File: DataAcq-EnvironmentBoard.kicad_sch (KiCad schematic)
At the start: 13 parts, among them J1 CAN Output, J2 CAN Input, U1 SHT45, U2 FS3000-1005, U3 LMT87DCK, U4 Daughterboard Connector

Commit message: initial layout/routing
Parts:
- added MH1, MH2, MH3, MH4: M.3, MountingHole:MountingHole_3mm, symbol Mechanical:MountingHole
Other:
- moved on the sheet: C1, C2, C3, C4, C5, C6, J1, J2, R1, U1, U2, U3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

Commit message: layout again
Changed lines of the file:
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@@
 	(wire
 		(pts
-			(xy 95.25 115.57) (xy 106.68 115.57)
+			(xy 101.6 115.57) (xy 106.68 115.57)
 		)
 		(stroke
@@
 	(wire
 		(pts
+			(xy 173.99 123.19) (xy 186.69 123.19)
+		)
+		(stroke
+			(width 0)
+			(type default)
+		)
+	)
+	(wire
+		(pts
 			(xy 151.13 60.96) (xy 166.37 60.96)
 		)
@@
 	(wire
 		(pts
-			(xy 177.8 123.19) (xy 186.69 123.19)
-		)
-		(stroke
-			(width 0)
-			(type default)
-		)
-	)
-	(wire
-		(pts
 			(xy 95.25 128.27) (xy 106.68 128.27)
 		)
@@
 	(wire
 		(pts
-			(xy 158.75 63.5) (xy 151.13 63.5)
+			(xy 173.99 139.7) (xy 186.69 139.7)
 		)
 		(stroke
@@
 	(wire
 		(pts
-			(xy 85.09 58.42) (xy 85.09 59.69)
+			(xy 158.75 63.5) (xy 151.13 63.5)
 		)
 		(stroke
@@
 	(wire
 		(pts
-			(xy 97.79 69.85) (xy 107.95 69.85)
+			(xy 85.09 58.42) (xy 85.09 59.69)
 		)
 		(stroke
@@
 	(wire
 		(pts
-			(xy 177.8 139.7) (xy 186.69 139.7)
+			(xy 97.79 69.85) (xy 107.95 69.85)
 		)
 		(stroke
@@
 		)
 	)
-	(label "+12V_In"
-		(at 177.8 123.19 0)
-		(fields_autoplaced yes)
-		(effects
-			(font
-				(size 1.27 1.27)
-			)
-			(justify left bottom)
-		)
-	)
 	(label "TEMP_OUT"
 		(at 228.6 62.23 0)
@@
 		)
 	)
-	(label "+12V_In"
-		(at 95.25 118.11 0)
-		(fields_autoplaced yes)
-		(effects
-			(font
-				(size 1.27 1.27)
-			)
-			(justify left bottom)
-		)
-	)
 	(label "PA1(ADC)"
 		(at 95.25 120.65 0)
@@
 	)
 	(symbol
+		(lib_id "power:+12V")
+		(at 95.25 118.11 90)
+		(unit 1)
+		(exclude_from_sim no)
+		(in_bom yes)
+		(on_board yes)
+		(dnp no)
+		(fields_autoplaced yes)
+		(property "Reference" "#PWR017"
+			(at 99.06 118.11 0)
+			(effects
+				(font
+					(size 1.27 1.27)
+				)
+				(hide yes)
+			)
+		)
+		(property "Value" "+12V_In"
+			(at 91.44 118.1099 90)
+			(effects
+				(font
+					(size 1.27 1.27)
+				)
+				(justify left)
+			)
+		)
+		(property "Footprint" ""
+			(at 95.25 118.11 0)
+			(effects
+				(font
+					(size 1.27 1.27)
+				)
+				(hide yes)
+			)
+		)
+		(property "Datasheet" ""
+			(at 95.25 118.11 0)
+			(effects
+				(font
+					(size 1.27 1.27)
+				)
+				(hide yes)
+			)
+		)
+		(property "Description" "Power symbol creates a global label with name \"+12V\""
+			(at 95.25 118.11 0)
+			(effects
+				(font
+					(size 1.27 1.27)
+				)
+				(hide yes)
+			)
+		)
+		(pin "1"
+		)
+		(instances
+			(project ""
+				(path "/bc5fb1f8-c603-414b-89d1-18cc156ddb66"
+					(reference "#PWR017")
+					(unit 1)
+				)
+			)
+		)
+	)
+	(symbol
 		(lib_id "power:+3.3V")
 		(at 152.4 133.35 270)
@@
 	)
 	(symbol
+		(lib_id "power:+12V")
+		(at 173.99 123.19 90)
+		(unit 1)
+		(exclude_from_sim no)
+		(in_bom yes)
+		(on_board yes)
+		(dnp no)
+		(fields_autoplaced yes)
+		(property "Reference" "#PWR018"
+			(at 177.8 123.19 0)
+			(effects
+				(font
+					(size 1.27 1.27)
+				)
+				(hide yes)
+			)
+		)
+		(property "Value" "+12V_In"
+			(at 170.18 123.1899 90)
+			(effects
+				(font
+					(size 1.27 1.27)
+				)
+				(justify left)
+			)
+		)
+		(property "Footprint" ""
+			(at 173.99 123.19 0)
+			(effects
+				(font
+					(size 1.27 1.27)
+				)
+				(hide yes)
+			)
+		)
+		(property "Datasheet" ""
+			(at 173.99 123.19 0)
+			(effects
+				(font
+					(size 1.27 1.27)
+				)
+				(hide yes)
+			)
+		)
+		(property "Description" "Power symbol creates a global label with name \"+12V\""
+			(at 173.99 123.19 0)
+			(effects
+				(font
+					(size 1.27 1.27)
+				)
+				(hide yes)
+			)
+		)
+		(pin "1"
+		)
+		(instances
+			(project "DataAcq-EnvironmentBoard"
+				(path "/bc5fb1f8-c603-414b-89d1-18cc156ddb66"
+					(reference "#PWR018")
+					(unit 1)
+				)
+			)
+		)
+	)
+	(symbol
 		(lib_id "power:VDDA")
 		(at 96.52 133.35 90)
@@
 	(symbol
 		(lib_id "power:GNDPWR")
-		(at 95.25 115.57 270)
+		(at 101.6 115.57 270)
 		(unit 1)
 		(exclude_from_sim no)
@@
 		(fields_autoplaced yes)
 		(property "Reference" "#PWR08"
-			(at 90.17 115.57 0)
+			(at 96.52 115.57 0)
 			(effects
 				(font
@@
 		)
 		(property "Value" "GNDPWR"
-			(at 91.44 115.4429 90)
+			(at 97.79 115.4429 90)
 			(effects
 				(font
@@
 		)
 		(property "Footprint" ""
-			(at 93.98 115.57 0)
+			(at 100.33 115.57 0)
 			(effects
 				(font
@@
 		)
 		(property "Datasheet" ""
-			(at 93.98 115.57 0)
+			(at 100.33 115.57 0)
 			(effects
 				(font
@@
 		)
 		(property "Description" "Power symbol creates a global label with name \"GNDPWR\" , global ground"
-			(at 95.25 115.57 0)
+			(at 101.6 115.57 0)
 			(effects
 				(font
@@
 					(unit 1)
 				)
+			)
+		)
+	)
+	(symbol
+		(lib_id "power:+12V")
+		(at 173.99 139.7 90)
+		(unit 1)
+		(exclude_from_sim no)
+		(in_bom yes)
+		(on_board yes)
+		(dnp no)
+		(fields_autoplaced yes)
+		(property "Reference" "#PWR019"
+			(at 177.8 139.7 0)
+			(effects
+				(font
+					(size 1.27 1.27)
+				)
+				(hide yes)
+			)
+		)
+		(property "Value" "+12V_In"
+			(at 170.18 139.6999 90)
+			(effects
+				(font
+					(size 1.27 1.27)
+				)
+				(justify left)
+			)
+		)
+		(property "Footprint" ""
+			(at 173.99 139.7 0)
+			(effects
+				(font
+					(size 1.27 1.27)
+				)
+				(hide yes)
+			)
+		)
+		(property "Datasheet" ""
+			(at 173.99 139.7 0)
+			(effects
+				(font
+					(size 1.27 1.27)
+				)
+				(hide yes)
+			)
+		)
+		(property "Description" "Power symbol creates a global label with name \"+12V\""
+			(at 173.99 139.7 0)
+			(effects
+				(font
+					(size 1.27 1.27)
+				)
+				(hide yes)
+			)
+		)
+		(pin "1"
+		)
+		(instances
+			(project "DataAcq-EnvironmentBoard"
+				(path "/bc5fb1f8-c603-414b-89d1-18cc156ddb66"
+					(reference "#PWR019")
+					(unit 1)
+				)

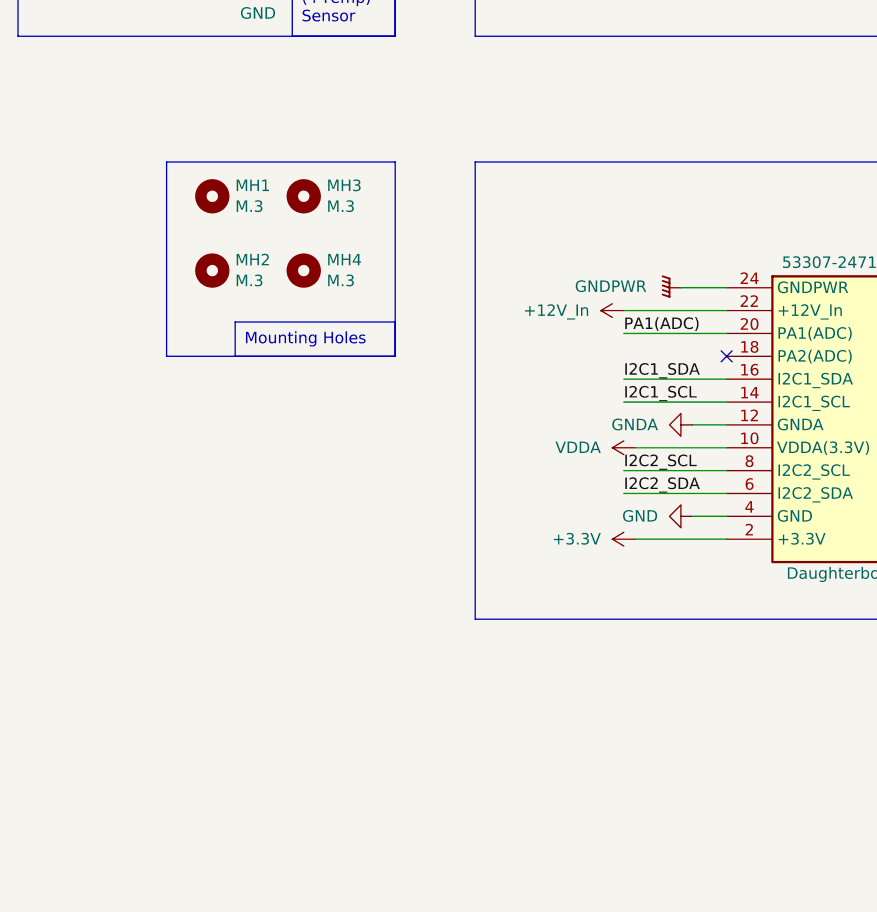
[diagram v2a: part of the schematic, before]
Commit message: add LEDs/testpoints to sch
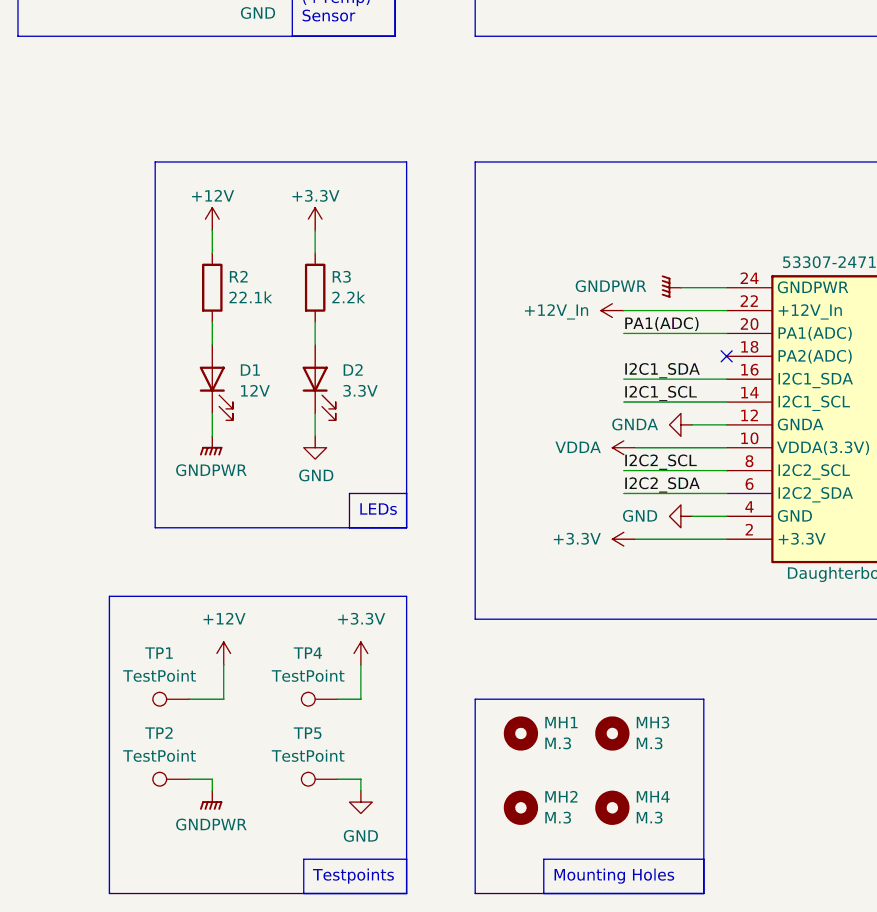
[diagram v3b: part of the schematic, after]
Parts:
- added D1: 12V, LED_SMD:LED_0805_2012Metric, symbol Device:LED
- added D2: 3.3V, LED_SMD:LED_0805_2012Metric, symbol Device:LED
- added R2: 22.1k, Resistor_SMD:R_0805_2012Metric, symbol Device:R
- added R3: 2.2k, Resistor_SMD:R_0805_2012Metric, symbol Device:R
- added TP1, TP2, TP4, TP5: TestPoint, Connector_PinHeader_2.54mm:PinHeader_1x01_P2.54mm_Vertical, symbol Connector:TestPoint
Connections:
- net +3.3V: now also R3.1, TP4.1
- net GND: now also D2.1 (K), TP5.1
- net GNDPWR: now also D1.1 (K), TP2.1
- new net: D1.2 (A), R2.2
- new net: D2.2 (A), R3.2
- new net +12V: R2.1, TP1.1
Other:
- moved on the sheet: MH1, MH2, MH3, MH4

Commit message: test points
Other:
- moved on the sheet: D1, D2, J1, J2, MH1, MH2, MH3, MH4, R2, R3, TP1, TP2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

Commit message: part numbers smh
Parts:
- C1, C2, C3, C5: P/N (none) -> C0805C104M5RACTU
- C4, C6: P/N (none) -> C0805C105K5PACTU
- J1, J2: P/N (none) -> 436500244
- R1: value 800 -> 1k; P/N (none) -> CRCW08051K00FKEAC
- U1: P/N (none) -> SHT45-AD1B-R3
- U2: P/N (none) -> FS3000-1005
- U3: P/N (none) -> LMT87QDCKRQ1
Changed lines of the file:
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@@
 			)
 		)
+		(property "P/N" "436500244"
+			(at 191.77 130.81 0)
+			(effects
+				(font
+					(size 1.27 1.27)
+				)
+				(hide yes)
+			)
+		)
 		(pin "2"
 		)
@@
 			)
 		)
+		(property "P/N" "C0805C104M5RACTU"
+			(at 196.85 57.15 0)
+			(effects
+				(font
+					(size 1.27 1.27)
+				)
+				(hide yes)
+			)
+		)
 		(pin "1"
 		)
@@
 			)
 		)
+		(property "P/N" "C0805C105K5PACTU"
+			(at 250.19 68.58 0)
+			(effects
+				(font
+					(size 1.27 1.27)
+				)
+				(hide yes)
+			)
+		)
 		(pin "1"
 		)
@@
 			)
 		)
+		(property "P/N" "C0805C104M5RACTU"
+			(at 170.18 59.69 0)
+			(effects
+				(font
+					(size 1.27 1.27)
+				)
+				(hide yes)
+			)
+		)
 		(pin "1"
 		)
@@
 			)
 		)
-		(property "Value" "800"
+		(property "Value" "1k"
 			(at 242.57 64.516 90)
 			(effects
@@
 			)
 		)
+		(property "P/N" "CRCW08051K00FKEAC"
+			(at 242.57 62.23 0)
+			(effects
+				(font
+					(size 1.27 1.27)
+				)
+				(hide yes)
+			)
+		)
 		(pin "1"
 		)
@@
 			)
 		)
+		(property "P/N" "C0805C105K5PACTU"
+			(at 158.75 71.12 0)
+			(effects
+				(font
+					(size 1.27 1.27)
+				)
+				(hide yes)
+			)
+		)
 		(pin "1"
 		)
@@
 			)
 		)
+		(property "P/N" "LMT87QDCKRQ1"
+			(at 218.44 62.23 0)
+			(effects
+				(font
+					(size 1.27 1.27)
+				)
+				(hide yes)
+			)
+		)
 		(pin "3"
 		)
@@
 			)
 		)
+		(property "P/N" "SHT45-AD1B-R3 "
+			(at 52.07 69.85 0)
+			(effects
+				(font
+					(size 1.27 1.27)
+				)
+				(hide yes)
+			)
+		)
 		(pin "2"
 		)
@@
 			)
 		)
+		(property "P/N" "C0805C104M5RACTU"
+			(at 85.09 63.5 0)
+			(effects
+				(font
+					(size 1.27 1.27)
+				)
+				(hide yes)
+			)
+		)
 		(pin "2"
 		)
@@
 			)
 		)
+		(property "P/N" "436500244"
+			(at 191.77 114.3 0)
+			(effects
+				(font
+					(size 1.27 1.27)
+				)
+				(hide yes)
+			)
+		)
 		(pin "2"
 		)
@@
 			)
 		)
+		(property "P/N" "C0805C104M5RACTU"
+			(at 97.79 63.5 0)
+			(effects
+				(font
+					(size 1.27 1.27)
+				)
+				(hide yes)
+			)
+		)
 		(pin "2"
 		)
@@
 				(hide yes)
 			)
+		)
+		(property "P/N" "FS3000-1005"
+			(at 123.19 55.88 0)
+			(effects
+				(font
+					(size 1.27 1.27)
+				)
+				(hide yes)
+			)

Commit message: dumbass labels
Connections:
- net +12V is gone; now on net +12V_In: R2.1, TP1.1
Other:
- moved on the sheet: J1, J2, U4

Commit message: cap
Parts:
- added C7: 0.1uF, Capacitor_SMD:C_0805_2012Metric, symbol Device:C
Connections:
- net +3.3V: now also C7.1
- net GND: now also C7.2
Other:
- moved on the sheet: U1
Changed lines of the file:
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@@
 	)
 	(junction
+		(at 52.07 78.74)
+		(diameter 0)
+		(color 0 0 0 0)
+	)
+	(junction
 		(at 215.9 49.53)
 		(diameter 0)
 		(color 0 0 0 0)
 	)
+	(junction
+		(at 52.07 60.96)
+		(diameter 0)
+		(color 0 0 0 0)
+	)
 	(no_connect
 		(at 142.24 137.16)
@@
 	(wire
 		(pts
+			(xy 52.07 60.96) (xy 52.07 62.23)
+		)
+		(stroke
+			(width 0)
+			(type default)
+		)
+	)
+	(wire
+		(pts
 			(xy 172.72 116.84) (xy 185.42 116.84)
 		)
@@
 	(wire
 		(pts
-			(xy 34.29 72.39) (xy 44.45 72.39)
+			(xy 31.75 72.39) (xy 41.91 72.39)
 		)
 		(stroke
@@
 	(wire
 		(pts
-			(xy 54.61 77.47) (xy 54.61 80.01)
+			(xy 52.07 77.47) (xy 52.07 78.74)
+		)
+		(stroke
+			(width 0)
+			(type default)
+		)
+	)
+	(wire
+		(pts
+			(xy 59.69 78.74) (xy 52.07 78.74)
 		)
 		(stroke
@@
 	(wire
 		(pts
+			(xy 59.69 73.66) (xy 59.69 78.74)
+		)
+		(stroke
+			(width 0)
+			(type default)
+		)
+	)
+	(wire
+		(pts
+			(xy 59.69 66.04) (xy 59.69 60.96)
+		)
+		(stroke
+			(width 0)
+			(type default)
+		)
+	)
+	(wire
+		(pts
 			(xy 250.19 62.23) (xy 261.62 62.23)
 		)
@@
 	(wire
 		(pts
-			(xy 34.29 67.31) (xy 44.45 67.31)
+			(xy 31.75 67.31) (xy 41.91 67.31)
 		)
 		(stroke
@@
 	(wire
 		(pts
+			(xy 59.69 60.96) (xy 52.07 60.96)
+		)
+		(stroke
+			(width 0)
+			(type default)
+		)
+	)
+	(wire
+		(pts
 			(xy 97.79 55.88) (xy 123.19 55.88)
 		)
@@
 	(wire
 		(pts
+			(xy 52.07 78.74) (xy 52.07 80.01)
+		)
+		(stroke
+			(width 0)
+			(type default)
+		)
+	)
+	(wire
+		(pts
 			(xy 218.44 49.53) (xy 218.44 54.61)
 		)
@@
 	(wire
 		(pts
-			(xy 54.61 59.69) (xy 54.61 62.23)
+			(xy 52.07 59.69) (xy 52.07 60.96)
 		)
 		(stroke
@@
 	(rectangle
 		(start 27.94 52.07)
-		(end 69.85 87.63)
+		(end 74.93 87.63)
 		(stroke
 			(width 0)
@@
 	(text_box "SHT45 Humidity (+Temp) Sensor\n"
 		(exclude_from_sim no)
-		(at 58.42 77.47 0)
+		(at 63.5 77.47 0)
 		(size 11.43 10.16)
 		(stroke
@@
 	)
 	(label "I2C1_SCL"
-		(at 34.29 67.31 0)
+		(at 31.75 67.31 0)
 		(fields_autoplaced yes)
 		(effects
@@
 	)
 	(label "I2C1_SDA"
-		(at 34.29 72.39 0)
+		(at 31.75 72.39 0)
 		(fields_autoplaced yes)
 		(effects
@@
 	(symbol
 		(lib_id "power:GND")
-		(at 54.61 80.01 0)
+		(at 52.07 80.01 0)
 		(unit 1)
 		(exclude_from_sim no)
@@
 		(fields_autoplaced yes)
 		(property "Reference" "#PWR01"
-			(at 54.61 86.36 0)
+			(at 52.07 86.36 0)
 			(effects
 				(font
@@
 		)
 		(property "Value" "GND"
-			(at 54.61 85.09 0)
+			(at 52.07 85.09 0)
 			(effects
 				(font
@@
 		)
 		(property "Footprint" ""
-			(at 54.61 80.01 0)
+			(at 52.07 80.01 0)
 			(effects
 				(font
@@
 		)
 		(property "Datasheet" ""
-			(at 54.61 80.01 0)
+			(at 52.07 80.01 0)
 			(effects
 				(font
@@
 		)
 		(property "Description" "Power symbol creates a global label with name \"GND\" , ground"
-			(at 54.61 80.01 0)
+			(at 52.07 80.01 0)
 			(effects
 				(font
@@
 	(symbol
 		(lib_id "Sensor_Humidity:SHT4x")
-		(at 52.07 69.85 0)
+		(at 49.53 69.85 0)
 		(unit 1)
 		(exclude_from_sim no)
@@
 		(dnp no)
 		(property "Reference" "U1"
-			(at 44.704 63.246 0)
+			(at 42.164 63.246 0)
 			(effects
 				(font
@@
 		)
 		(property "Value" "SHT45"
-			(at 44.45 76.454 0)
+			(at 41.91 76.454 0)
 			(effects
 				(font
@@
 		)
 		(property "Footprint" "Sensor_Humidity:Sensirion_DFN-4_1.5x1.5mm_P0.8mm_SHT4x_NoCentralPad"
-			(at 55.88 76.2 0)
+			(at 53.34 76.2 0)
 			(effects
 				(font
@@
 		)
 		(property "Datasheet" "https://sensirion.com/media/documents/33FD6951/624C4357/Datasheet_SHT4x.pdf"
-			(at 55.88 78.74 0)
+			(at 53.34 78.74 0)
 			(effects
 				(font
@@
 		)
 		(property "Description" "Digital Humidity and Temperature Sensor, +/-1%RH, +/-0.1degC, I2C, 1.08-3.6V, 16bit, DFN-4"
-			(at 52.07 69.85 0)
+			(at 49.53 69.85 0)
 			(effects
 				(font
@@
 		)
 		(property "P/N" "SHT45-AD1B-R3 "
-			(at 52.07 69.85 0)
+			(at 49.53 69.85 0)
 			(effects
 				(font
@@
 	(symbol
 		(lib_id "power:+3.3V")
-		(at 54.61 59.69 0)
+		(at 52.07 59.69 0)
 		(unit 1)
 		(exclude_from_sim no)
@@
 		(fields_autoplaced yes)
 		(property "Reference" "#PWR02"
-			(at 54.61 63.5 0)
+			(at 52.07 63.5 0)
 			(effects
 				(font
@@
 		)
 		(property "Value" "+3.3V"
-			(at 54.61 54.61 0)
+			(at 52.07 54.61 0)
 			(effects
 				(font
@@
 		)
 		(property "Footprint" ""
-			(at 54.61 59.69 0)
+			(at 52.07 59.69 0)
 			(effects
 				(font
@@
 		)
 		(property "Datasheet" ""
-			(at 54.61 59.69 0)
+			(at 52.07 59.69 0)
 			(effects
 				(font
@@
 		)
 		(property "Description" "Power symbol creates a global label with name \"+3.3V\""
-			(at 54.61 59.69 0)
+			(at 52.07 59.69 0)
 			(effects
 				(font
@@
 					(unit 1)
 				)
+			)
+		)
+	)
+	(symbol
+		(lib_id "Device:C")
+		(at 59.69 69.85 0)
+		(unit 1)
+		(exclude_from_sim no)
+		(in_bom yes)
+		(on_board yes)
+		(dnp no)
+		(fields_autoplaced yes)
+		(property "Reference" "C7"
+			(at 63.5 68.5799 0)
+			(effects
+				(font
+					(size 1.27 1.27)
+				)
+				(justify left)
+			)
+		)
+		(property "Value" "0.1uF"
+			(at 63.5 71.1199 0)
+			(effects
+				(font
+					(size 1.27 1.27)
+				)
+				(justify left)
+			)
+		)
+		(property "Footprint" "Capacitor_SMD:C_0805_2012Metric"
+			(at 60.6552 73.66 0)
+			(effects
+				(font
+					(size 1.27 1.27)
+				)
+				(hide yes)
+			)
+		)
+		(property "Datasheet" "~"
+			(at 59.69 69.85 0)
+			(effects
+				(font
+					(size 1.27 1.27)
+				)
+				(hide yes)
+			)
+		)
+		(property "Description" "Unpolarized capacitor"
+			(at 59.69 69.85 0)
+			(effects
+				(font
+					(size 1.27 1.27)
+				)
+				(hide yes)
+			)
+		)
+		(property "P/N" "C0805C104M5RACTU"
+			(at 59.69 69.85 0)
+			(effects
+				(font
+					(size 1.27 1.27)
+				)
+				(hide yes)
+			)
+		)
+		(pin "2"
+		)
+		(pin "1"
+		)
+		(instances
+			(project "DataAcq-EnvironmentBoard"
+				(path "/bc5fb1f8-c603-414b-89d1-18cc156ddb66"
+					(reference "C7")
+					(unit 1)
+				)

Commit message: third times the charm (layout)
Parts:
- removed MH1, MH2, MH3, MH4: M.3, MountingHole:MountingHole_3mm, symbol Mechanical:MountingHole
- TP1, TP2, TP4, TP5: footprint Connector_PinHeader_2.54mm:PinHeader_1x01_P2.54mm_Vertical -> UTSVT_Special:TestPoint_HEX_3mmID
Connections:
- net GND: no longer J1.3 (Pin_3), J2.3 (Pin_3)
- net GNDPWR: now also J1.3 (Pin_3), J2.3 (Pin_3)
